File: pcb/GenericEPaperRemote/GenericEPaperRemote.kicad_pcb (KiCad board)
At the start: 2 copper layers, 190.5 x 61 mm, 112 parts, among them J1 Display, J2 speaker, J3 Prog, J4 JTAG, J5 Barrel_Jack, Q1 BC817, Q2 BC817, SW1 TactileSwitchSMD6x6, SW10 TactileSwitchSMD6x6, SW11 Rotary_Encoder_Switch, SW12 reset, SW13 bootloader, SW14 Conn_01x02_Male, SW2 TactileSwitchSMD6x6, SW3 TactileSwitchSMD6x6, SW4 TactileSwitchSMD6x6, SW5 TactileSwitchSMD6x6, SW6 TactileSwitchSMD6x6, SW7 TactileSwitchSMD6x6, SW8 TactileSwitchSMD6x6, SW9 TactileSwitchSMD6x6, U1 ESP32-WROVER-B_(16MB), U2 FT232RL, U3 NCP1117ST33T3G

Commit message: Finalize first version of pcb
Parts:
- added Logo: OSSLogo, codingfragment-components:OSSLogo, F.Cu at (261.9, 104.9)
- moved TP10 56.8 mm to (160.0, 118.9)
- moved TP11 56.5 mm to (156.0, 118.9)
- moved TP12 56.4 mm to (151.9, 118.9)
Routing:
- net /io_sel2: track 0.00 -> 261.3 mm, vias 0 -> 3
- net /io_sel0: track 0.00 -> 217.7 mm, vias 0 -> 9
- net /io_in0: track 33.4 -> 186.4 mm, vias 2 -> 8
- net /io_in1: track 34.8 -> 187.7 mm, vias 2 -> 12
- net /io_in2: track 36.2 -> 182.9 mm, vias 2 -> 8
- net /io_sel1: track 0.00 -> 137.5 mm, vias 0 -> 3
- net /io_in3: track 37.5 -> 170.7 mm, vias 2 -> 5
- net /IO0: track 47.8 -> 149.2 mm, vias 1 -> 6
- net GND: track 0.63 -> 35.8 mm, vias 0 -> 156
- net /io_rot_b: track 0.00 -> 25.7 mm, vias 0 -> 1
- net Net-(D9-Pad2): track 0.00 -> 16.3 mm
- net Net-(D10-Pad2): track 0.00 -> 16.1 mm, vias 0 -> 2
- net Net-(D11-Pad2): track 0.00 -> 15.8 mm, vias 0 -> 1
- net Net-(D8-Pad2): track 0.00 -> 14.0 mm
- net Net-(D6-Pad2): track 0.00 -> 14.0 mm
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- added copper zone on B.Cu, net GND
- added copper zone on F.Cu, net GND
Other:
- board text added: "+5V Input"
- board text added: "3V3"
- board text added: "3V3 FT232"
- board text added: "3V3 RX TX RTS DTR GND"
- board text added: "AUX Switch"
- board text added: "BL Latch IO0"
- board text added: "Boot Latch IO 0"
- board text added: "Cut to disable USB-to-seriell"
- board text added: "EN ESP32"
- board text added: "IO Sel 0"
- board text added: "IO Sel 1"
- board text added: "IO Sel 2"
- board text added: "JTAG GND .. +3V3 X|TDI|TD0|TCK|TMS"
- board text added: "Prog"
- board text added: "RX"
- board text added: "Reset"
- board text added: "Seriell Prog RX|TX|EN IO0|GND|+3V3"
- board text added: "Speaker"
- board text added: "TX"
- board text added: "generic ESP32 Remote v0.5 Codingfragments 2020 Stefan Marx stefan@marx-merten.de"

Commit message: small changes
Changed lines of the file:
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@@
     (38 B.Mask user)
     (39 F.Mask user)
-    (40 Dwgs.User user)
+    (40 Dwgs.User user hide)
     (41 Cmts.User user)
     (42 Eco1.User user)
@@
   (segment (start 135.66 101.6) (end 135.58 101.68) (width 0.2) (layer Front) (net 42))
   (segment (start 139.446 101.6) (end 135.66 101.6) (width 0.2) (layer Front) (net 42))
-  (via (at 142.494 103.886) (size 0.6) (drill 0.3) (layers Front Back) (net 43))
-  (segment (start 142.288 103.68) (end 142.494 103.886) (width 0.2) (layer Front) (net 43))
-  (segment (start 135.58 103.68) (end 142.288 103.68) (width 0.2) (layer Front) (net 43))
-  (segment (start 142.494 103.886) (end 144.018 102.362) (width 0.2) (layer Back) (net 43))
-  (segment (start 144.018 102.362) (end 197.72938 102.362) (width 0.2) (layer Back) (net 43))
   (segment (start 201.67138 98.42) (end 213.75 98.42) (width 0.2) (layer Back) (net 43))
   (segment (start 197.72938 102.362) (end 201.67138 98.42) (width 0.2) (layer Back) (net 43))
+  (segment (start 144.018 102.362) (end 197.72938 102.362) (width 0.2) (layer Back) (net 43))
+  (segment (start 142.494 103.505) (end 144.018 102.362) (width 0.2) (layer Back) (net 43))
+  (segment (start 142.288 103.68) (end 135.58 103.68) (width 0.2) (layer Front) (net 43))
+  (segment (start 142.494 103.505) (end 142.288 103.68) (width 0.2) (layer Front) (net 43))
+  (via (at 142.494 103.505) (size 0.6) (drill 0.3) (layers Front Back) (net 43))
   (via (at 142.494 105.664) (size 0.6) (drill 0.3) (layers Front Back) (net 44))
   (segment (start 142.478 105.68) (end 142.494 105.664) (width 0.2) (layer Front) (net 44))
@@
     (connect_pads (clearance 0.508))
     (min_thickness 0.254)
-    (fill (arc_segments 32) (thermal_gap 0.508) (thermal_bridge_width 0.508))
+    (fill yes (arc_segments 32) (thermal_gap 0.508) (thermal_bridge_width 0.508))
     (polygon
       (pts
@@
     (connect_pads (clearance 0.508))
     (min_thickness 0.254)
-    (fill (arc_segments 32) (thermal_gap 0.508) (thermal_bridge_width 0.508))
+    (fill yes (arc_segments 32) (thermal_gap 0.508) (thermal_bridge_width 0.508))
     (polygon
       (pts

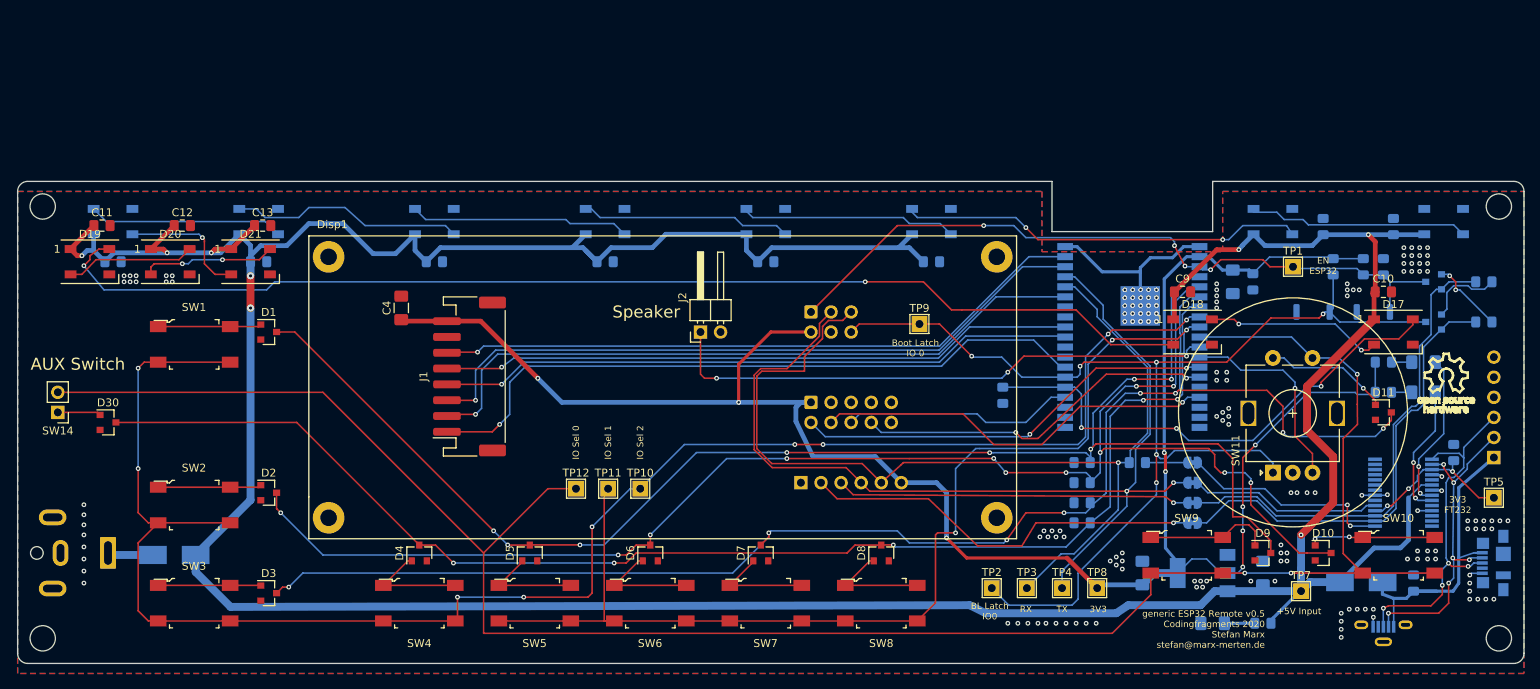
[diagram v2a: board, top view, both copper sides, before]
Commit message: Added pullups for encoder and switch away from io0 to prevent boot to root-loader when rotary encoder pulls low)
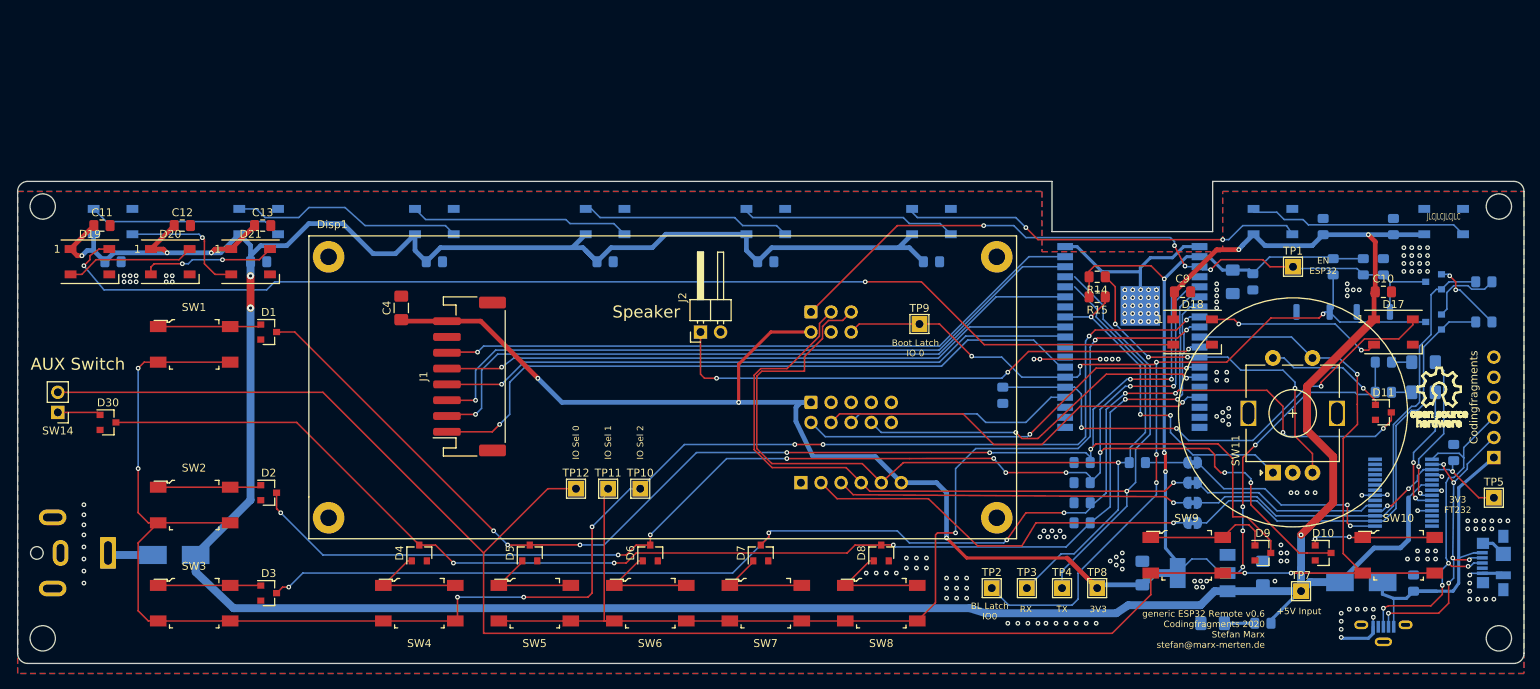
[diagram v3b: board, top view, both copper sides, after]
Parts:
- removed Logo: OSSLogo, codingfragment-components:OSSLogo
- added LOGO1: Codingfragments, codingfragment-components:OSSLogo, F.Cu at (261.0, 106.7)
- added R14: 10K, Resistor_SMD:R_0805_2012Metric_Pad1.15x1.40mm_HandSolder, F.Cu at (217.8, 92.1)
- added R15: 10K, Resistor_SMD:R_0805_2012Metric_Pad1.15x1.40mm_HandSolder, F.Cu at (217.8, 94.6)
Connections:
- SW11 pad A: /IO0 -> /io_rot_a
- U1 pad 31: Net-(U1-Pad31) -> /io_rot_a
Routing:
- net /io_rot_a: track 0.00 -> 42.5 mm, vias 0 -> 3
- net GND: track 35.8 -> 56.5 mm, vias 156 -> 179
- net /io_rot_b: track 25.7 -> 44.6 mm, vias 1 -> 4
- net /IO0: track 149.2 -> 132.0 mm
- net +3V3: track 252.2 -> 265.9 mm, vias 9 -> 11
- net /esp_rx: track 126.1 -> 124.8 mm
- net /io_sel0: track 217.7 -> 218.9 mm
- net /esp_tx: track 129.9 -> 128.7 mm
- net /io_sel1: track 137.5 -> 138.7 mm
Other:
- board text added: "JLCJLCJLCJLC"
- board text added: "generic ESP32 Remote v0.6 Codingfragments 2020 Stefan Marx stefan@marx-merten.de"
- board text removed: "generic ESP32 Remote v0.5 Codingfragments 2020 Stefan Marx stefan@marx-merten.de"

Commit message: added extension pins for ws2812b
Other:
- board text added: "+5V OK"

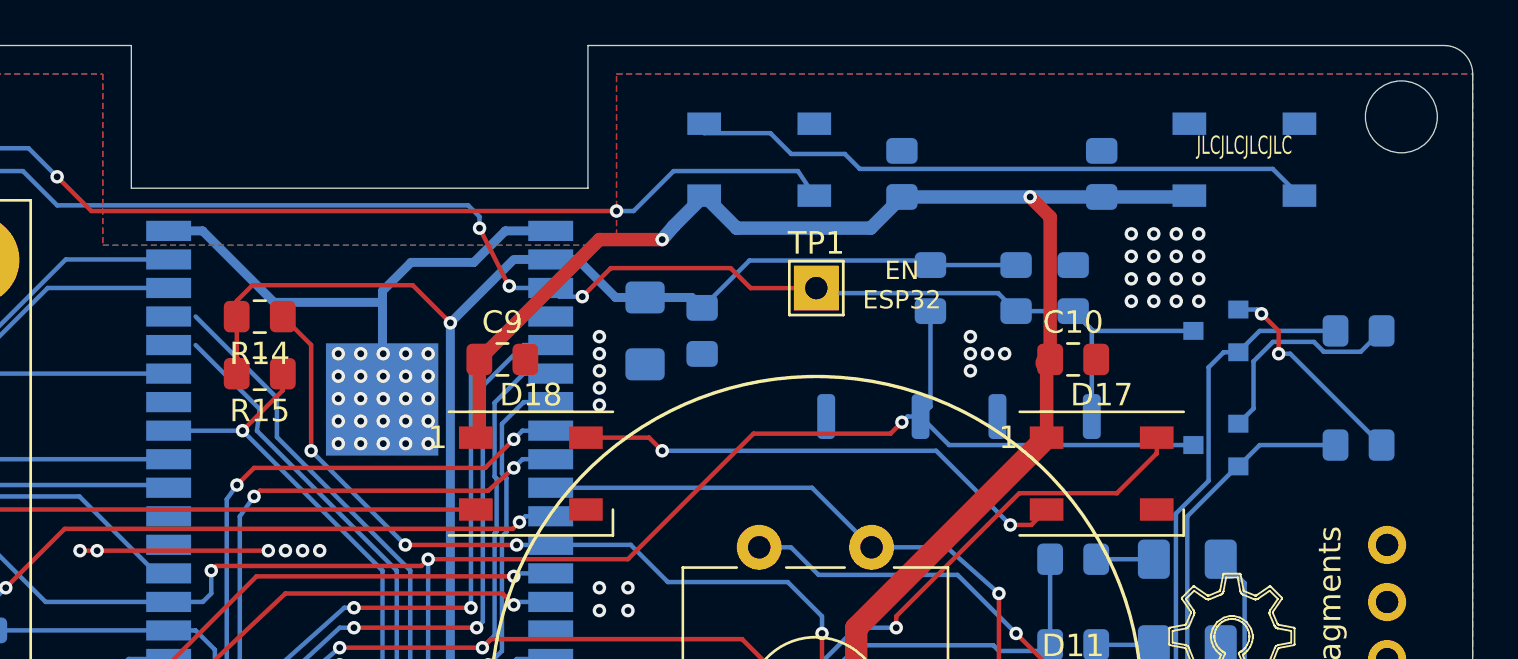
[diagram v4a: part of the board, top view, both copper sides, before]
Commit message: added aux ws2812B Socket (J6)
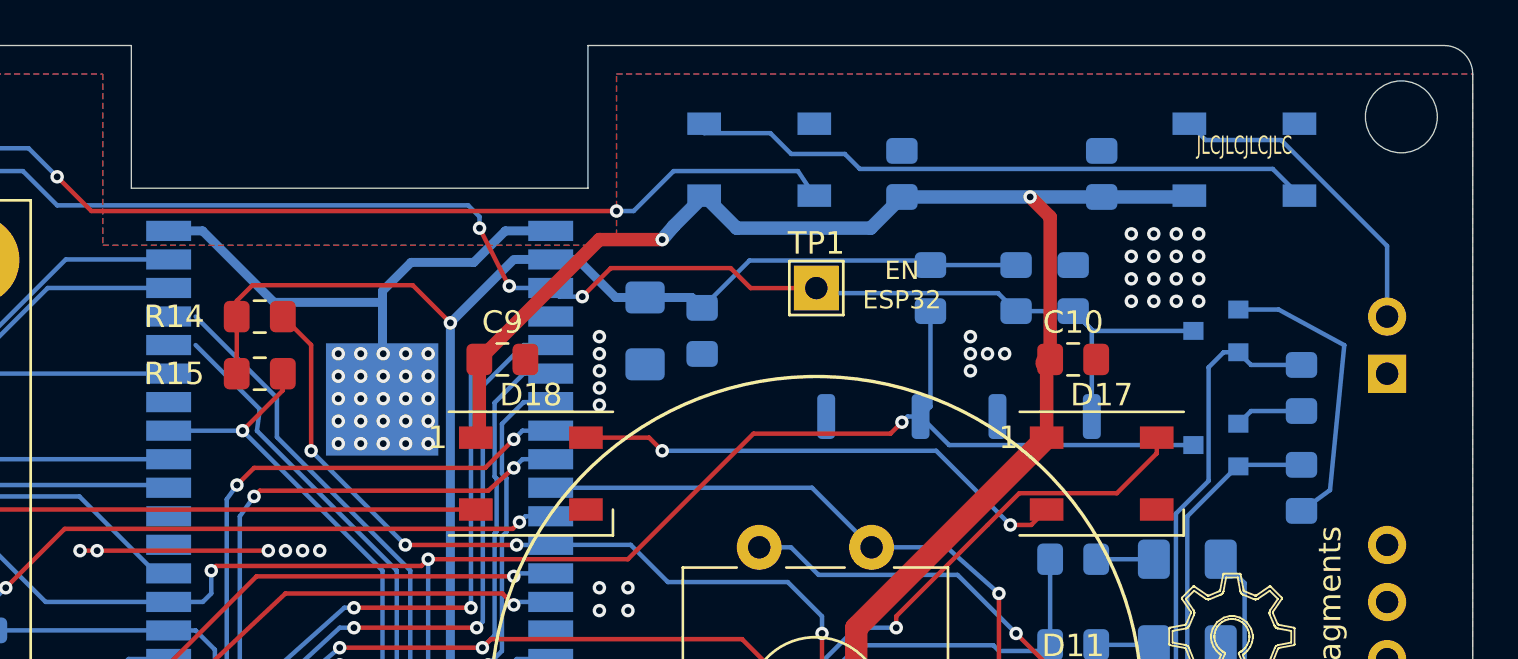
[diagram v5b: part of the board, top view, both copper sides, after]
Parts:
- added J6: Conn_01x02_Male, Connector_PinHeader_2.54mm:PinHeader_1x02_P2.54mm_Vertical, B.Cu at (268.0, 94.6)
- moved R12 3.59 mm to (264.2, 95.2), turned to 90 degrees
- moved R11 3.17 mm to (264.2, 99.7), turned to 90 degrees
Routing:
- net Net-(D29-Pad2): track 0.00 -> 14.2 mm
- net Net-(Q2-Pad1): track 9.68 -> 3.04 mm
- net Net-(Q1-Pad1): track 9.47 -> 13.2 mm, vias 2 -> 0
- net /Connectors/DTR: track 58.5 -> 56.6 mm
- net /Connectors/RTS: track 61.9 -> 60.2 mm
